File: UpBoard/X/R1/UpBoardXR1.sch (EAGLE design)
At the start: 59 parts, among them CN1 100nF, CN2 100nF, CN3 100nF, CN4 100nF, IC1 SAM3X8E(ARDUINO), IC2 W25N01GVZEIG/IT, Q1 FFB2222A, Q2 FFB2222A, X1 16POS_RIBBON, X2 16POS_RIBBON, X3 16POS_RIBBON, X4 16POS_RIBBON, Y1 FH1200001, Y2 ABS05

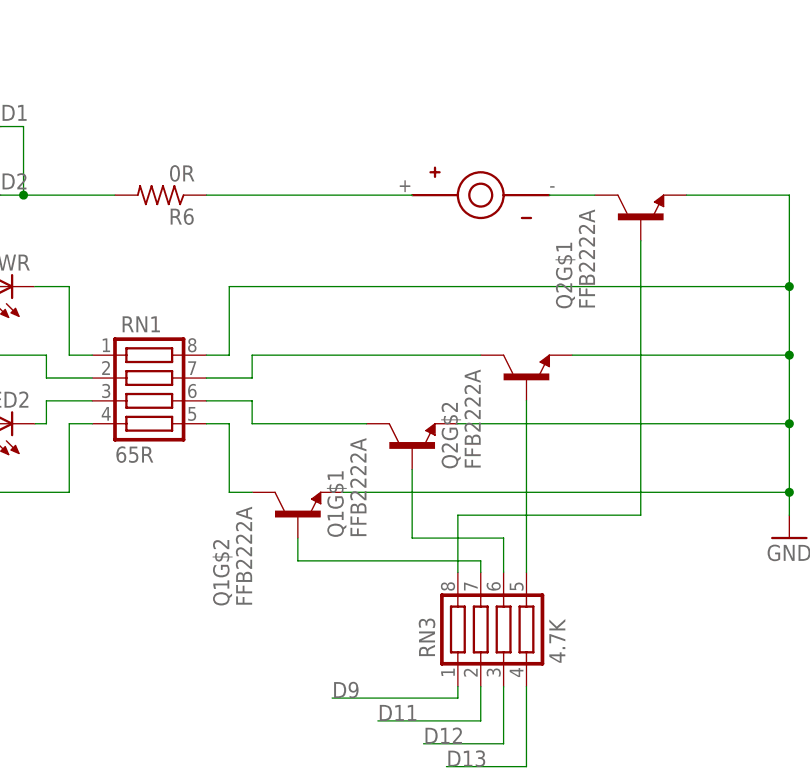
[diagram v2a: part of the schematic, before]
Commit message: Changed transistors
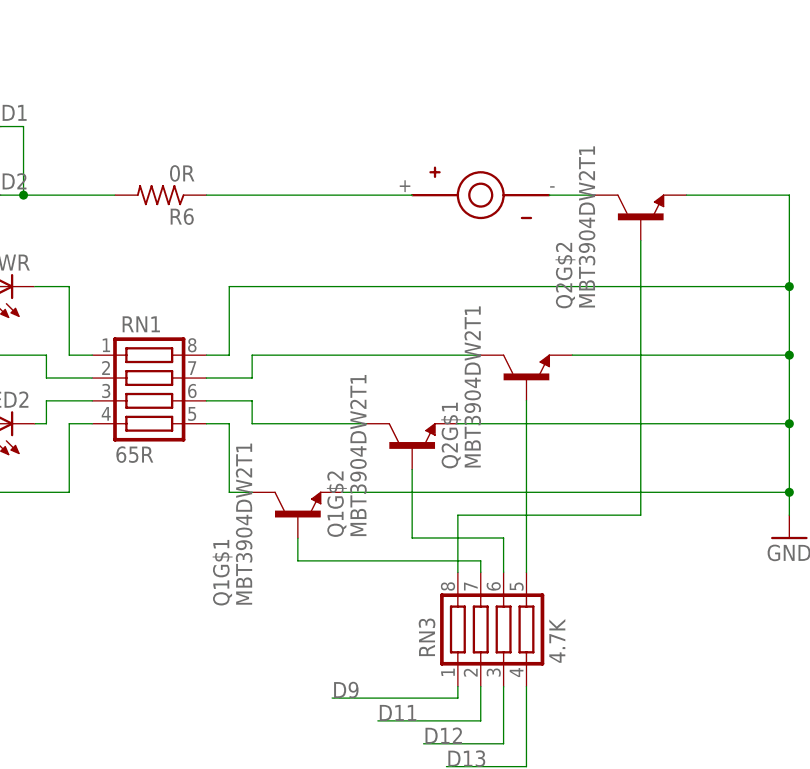
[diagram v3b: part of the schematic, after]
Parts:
- Q1, Q2: value FFB2222A -> MBT3904DW2T1; device CPSS_IC:FFB2222A -> CPSS_IC:MBT3904DW2T1
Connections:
- net N$10: now also Q2G$1.C; no longer Q2G$2.C
- net N$11: now also Q1G$2.C; no longer Q1G$1.C
- net N$12: now also Q1G$1.C; no longer Q1G$2.C
- net N$16: now also Q1G$2.B; no longer Q1G$1.B
- net N$17: now also Q1G$1.B; no longer Q1G$2.B
- net N$19: now also Q2G$2.B; no longer Q2G$1.B
- net N$33: now also Q2G$2.C; no longer Q2G$1.C
- net N$8: now also Q2G$1.B; no longer Q2G$2.B
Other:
- moved on the sheet: Q1G$1, Q1G$2, Q2G$1, Q2G$2
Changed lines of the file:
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@@
 <part name="SJ2" library="CPSS_CONNECTOR" deviceset="SOLBRDG" device=""/>
 <part name="RN3" library="resistor-net" library_urn="urn:adsk.eagle:library:343" deviceset="CTS742C083" device="" package3d_urn="urn:adsk.eagle:package:24985/1" value="4.7K"/>
-<part name="Q2" library="CPSS_IC" deviceset="FFB2222A" device=""/>
-<part name="Q1" library="CPSS_IC" deviceset="FFB2222A" device=""/>
+<part name="Q1" library="CPSS_IC" deviceset="MBT3904DW2T1" device=""/>
+<part name="Q2" library="CPSS_IC" deviceset="MBT3904DW2T1" device=""/>
 </parts>
 <sheets>
@@
 <instance part="SJ2" gate="G$1" x="270.51" y="168.91"/>
 <instance part="RN3" gate="G$1" x="330.2" y="201.93" rot="R90"/>
-<instance part="Q2" gate="G$1" x="347.98" y="248.92" rot="R90"/>
-<instance part="Q2" gate="G$2" x="335.28" y="231.14" rot="R90"/>
-<instance part="Q1" gate="G$1" x="322.58" y="223.52" rot="R90"/>
-<instance part="Q1" gate="G$2" x="309.88" y="215.9" rot="R90"/>
+<instance part="Q1" gate="G$1" x="309.88" y="215.9" rot="R90"/>
+<instance part="Q1" gate="G$2" x="322.58" y="223.52" rot="R90"/>
+<instance part="Q2" gate="G$1" x="335.28" y="231.14" rot="R90"/>
+<instance part="Q2" gate="G$2" x="347.98" y="248.92" rot="R90"/>
 </instances>
 <busses>
@@
 <junction x="364.49" y="218.44"/>
 <pinref part="GND3" gate="1" pin="GND"/>
-<pinref part="Q2" gate="G$2" pin="E"/>
-<pinref part="Q1" gate="G$1" pin="E"/>
-<pinref part="Q1" gate="G$2" pin="E"/>
 <wire x1="353.06" y1="251.46" x2="364.49" y2="251.46" width="0.1524" layer="91"/>
 <wire x1="364.49" y1="251.46" x2="364.49" y2="241.3" width="0.1524" layer="91"/>
@@
 <wire x1="302.26" y1="241.3" x2="364.49" y2="241.3" width="0.1524" layer="91"/>
 <junction x="364.49" y="241.3"/>
+<pinref part="Q1" gate="G$1" pin="E"/>
+<pinref part="Q1" gate="G$2" pin="E"/>
 <pinref part="Q2" gate="G$1" pin="E"/>
+<pinref part="Q2" gate="G$2" pin="E"/>
 </segment>
 <segment>
@@
 <wire x1="342.9" y1="251.46" x2="337.82" y2="251.46" width="0.1524" layer="91"/>
 <pinref part="LS1" gate="G$1" pin="-"/>
-<pinref part="Q2" gate="G$1" pin="C"/>
+<pinref part="Q2" gate="G$2" pin="C"/>
 </segment>
 </net>
@@
 <pinref part="RN1" gate="G$1" pin="7"/>
 <wire x1="304.8" y1="231.14" x2="299.72" y2="231.14" width="0.1524" layer="91"/>
-<pinref part="Q2" gate="G$2" pin="C"/>
+<pinref part="Q2" gate="G$1" pin="C"/>
 </segment>
 </net>
@@
 <wire x1="304.8" y1="228.6" x2="304.8" y2="226.06" width="0.1524" layer="91"/>
 <wire x1="304.8" y1="226.06" x2="317.5" y2="226.06" width="0.1524" layer="91"/>
-<pinref part="Q1" gate="G$1" pin="C"/>
+<pinref part="Q1" gate="G$2" pin="C"/>
 </segment>
 </net>
@@
 <wire x1="302.26" y1="226.06" x2="302.26" y2="218.44" width="0.1524" layer="91"/>
 <wire x1="302.26" y1="218.44" x2="304.8" y2="218.44" width="0.1524" layer="91"/>
-<pinref part="Q1" gate="G$2" pin="C"/>
+<pinref part="Q1" gate="G$1" pin="C"/>
 </segment>
 </net>
 <net name="N$16" class="0">
 <segment>
-<pinref part="Q1" gate="G$1" pin="B"/>
 <wire x1="322.58" y1="220.98" x2="322.58" y2="213.36" width="0.1524" layer="91"/>
 <wire x1="322.58" y1="213.36" x2="332.74" y2="213.36" width="0.1524" layer="91"/>
 <pinref part="RN3" gate="G$1" pin="6"/>
 <wire x1="332.74" y1="209.55" x2="332.74" y2="213.36" width="0.1524" layer="91"/>
+<pinref part="Q1" gate="G$2" pin="B"/>
 </segment>
 </net>
@@
 <segment>
 <wire x1="330.2" y1="210.82" x2="309.88" y2="210.82" width="0.1524" layer="91"/>
-<pinref part="Q1" gate="G$2" pin="B"/>
 <wire x1="309.88" y1="213.36" x2="309.88" y2="210.82" width="0.1524" layer="91"/>
 <pinref part="RN3" gate="G$1" pin="7"/>
 <wire x1="330.2" y1="209.55" x2="330.2" y2="210.82" width="0.1524" layer="91"/>
+<pinref part="Q1" gate="G$1" pin="B"/>
 </segment>
 </net>
 <net name="N$19" class="0">
 <segment>
-<pinref part="Q2" gate="G$1" pin="B"/>
 <pinref part="RN3" gate="G$1" pin="8"/>
 <wire x1="347.98" y1="215.9" x2="347.98" y2="246.38" width="0.1524" layer="91"/>
 <wire x1="327.66" y1="209.55" x2="327.66" y2="215.9" width="0.1524" layer="91"/>
 <wire x1="327.66" y1="215.9" x2="347.98" y2="215.9" width="0.1524" layer="91"/>
+<pinref part="Q2" gate="G$2" pin="B"/>
 </segment>
 </net>
@@
 <segment>
 <pinref part="RN3" gate="G$1" pin="5"/>
-<pinref part="Q2" gate="G$2" pin="B"/>
 <wire x1="335.28" y1="209.55" x2="335.28" y2="228.6" width="0.1524" layer="91"/>
+<pinref part="Q2" gate="G$1" pin="B"/>
 </segment>
 </net>
